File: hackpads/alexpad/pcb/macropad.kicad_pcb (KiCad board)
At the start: 2 copper layers, 86.2 x 100 mm, 93 parts, among them J1 USB_C_Receptacle_USB2.0_14P, J2 Conn_01x03, J3 Conn_01x04_Socket, M1 Vibration Motor, Q1 TM30N03ADF, SW1 RotaryEncoder_Switch, SW10 Cherry MX Blue, SW11 Cherry MX Blue, SW12 Cherry MX Blue, SW13 Cherry MX Blue, SW14 Cherry MX Blue, SW15 Cherry MX Blue, SW16 Cherry MX Blue, SW17 Cherry MX Blue, SW18 Cherry MX Blue, SW2 TS-1089S-02526, SW3 Cherry MX Blue, SW4 Cherry MX Blue, SW5 Cherry MX Blue, SW6 Cherry MX Blue, SW7 Cherry MX Blue, SW8 Cherry MX Blue, SW9 Cherry MX Blue, U1 RP2040, U2 AMS1117-3.3, U3 W25Q128JVS, U4 SN74LVC1T45DBV, Y1 Crystal_GND24

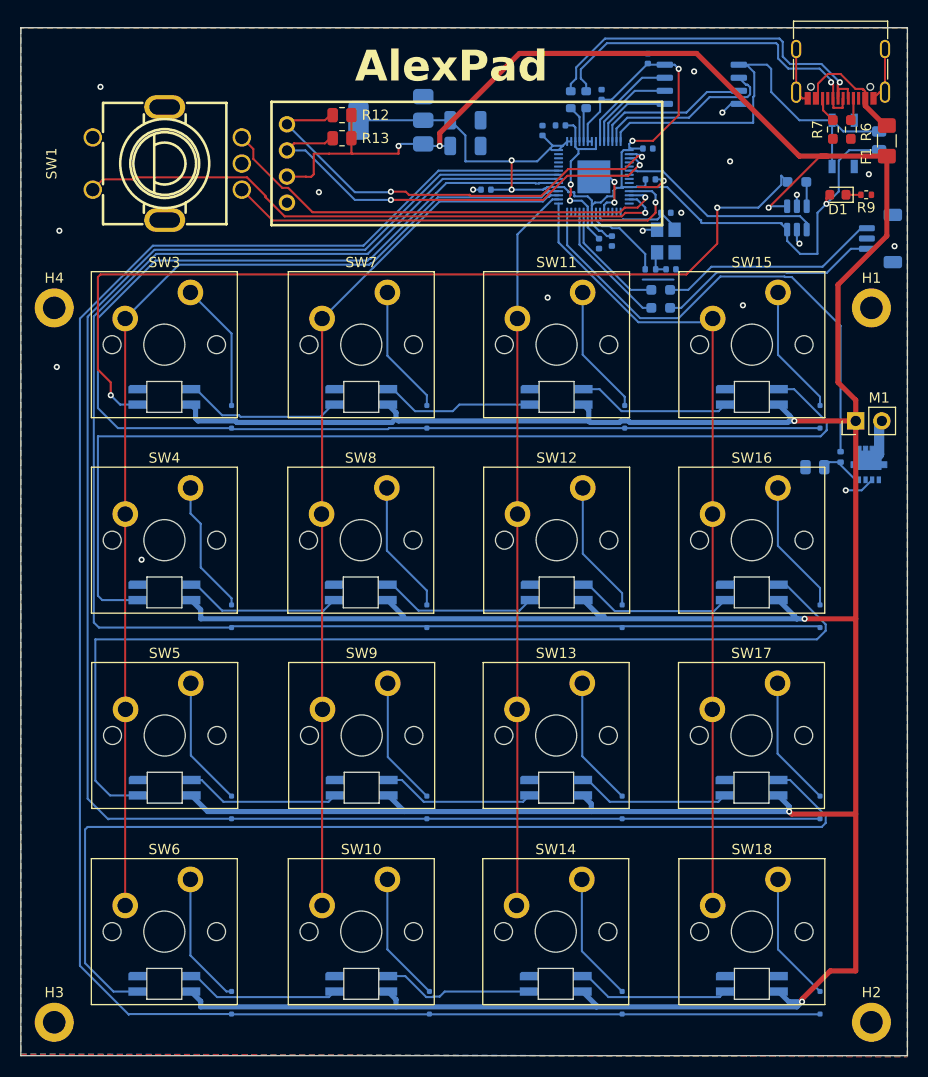
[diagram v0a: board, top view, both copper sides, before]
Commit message: update pcb to have buzzer
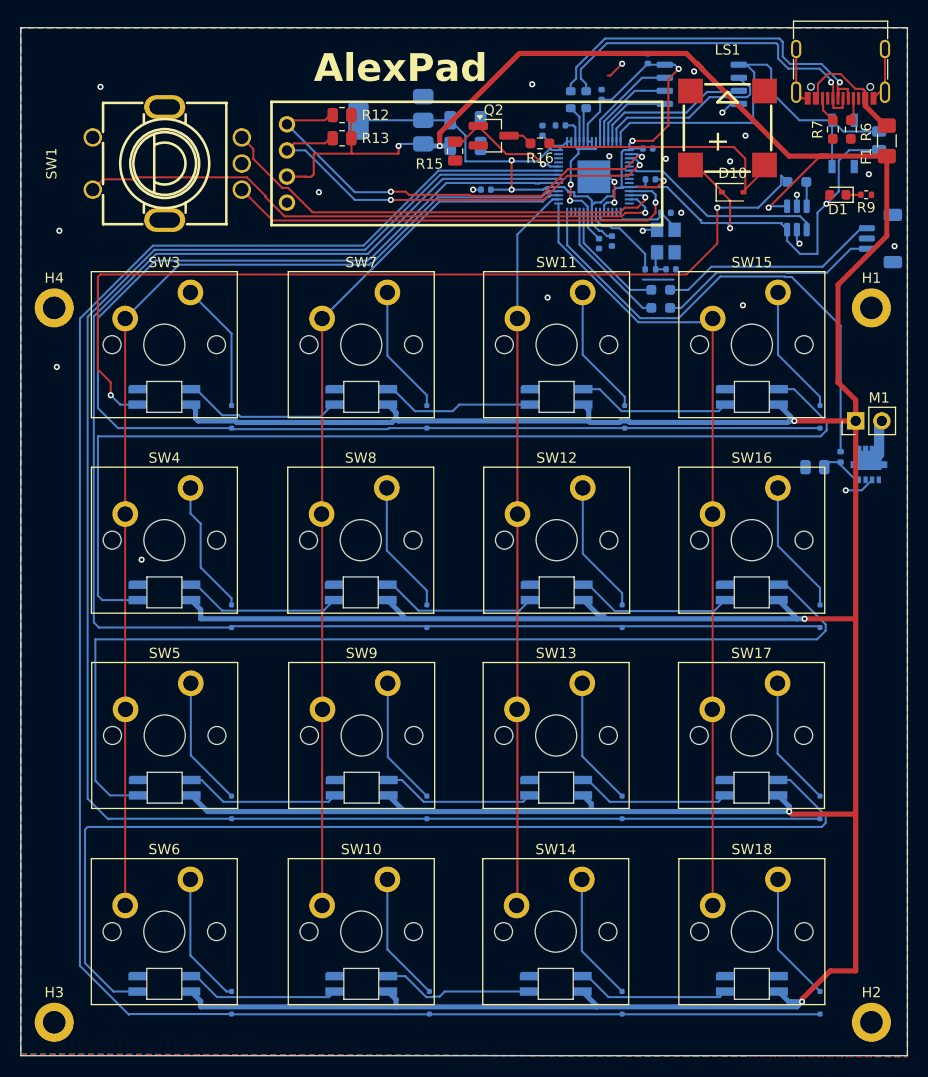
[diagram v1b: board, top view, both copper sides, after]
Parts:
- added D10: 1N4148WS, Diode_SMD:D_SOD-323, F.Cu at (173.5, 79.0)
- added LS1: Buzzer, easyeda2kicad:BUZ-SMD_4P-L8.5-W8.5-P8.50-BR, F.Cu at (173.0, 72.8)
- added Q2: Q_NMOS_GSD, Package_TO_SOT_SMD:SOT-23_Handsoldering, F.Cu at (150.2, 73.5)
- added R15: 10k, Resistor_SMD:R_0805_2012Metric, F.Cu at (146.5, 75.0)
- added R16: 10, Resistor_SMD:R_0603_1608Metric_Pad0.98x0.95mm_HandSolder, F.Cu at (154.8, 74.2)
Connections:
- U1 pad 38: unconnected-(U1-GPIO26_ADC0-Pad38) -> BUZZER
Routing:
- net Net-(D10-A): track 0.00 -> 26.3 mm
- net BUZZER: track 0.00 -> 12.3 mm, vias 0 -> 1
- net +3V3: track 119.0 -> 127.1 mm, vias 5 -> 6
- net Net-(Q2-D): track 0.00 -> 2.40 mm
- net GND: track 32.0 -> 33.9 mm, vias 21 -> 26
- net SDA: track 45.4 -> 44.8 mm
